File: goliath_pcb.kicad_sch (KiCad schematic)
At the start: 56 parts, among them IC1 MCT9001SD, IC2 MCT9001SD, IC3 MCT9001SD, IC4 MCT9001SD, IC5 MCT9001SD, IC6 MCT9001SD, IC7 MCT9001SD, J1 RJ45_LED, J2 RJ45_LED, J3 RJ45_LED, J4 RJ45_LED, U1 Pico, U2 LM7805_TO220, U3 74HCT244, U4 74HCT244, U5 LTC1298CS8-PBF

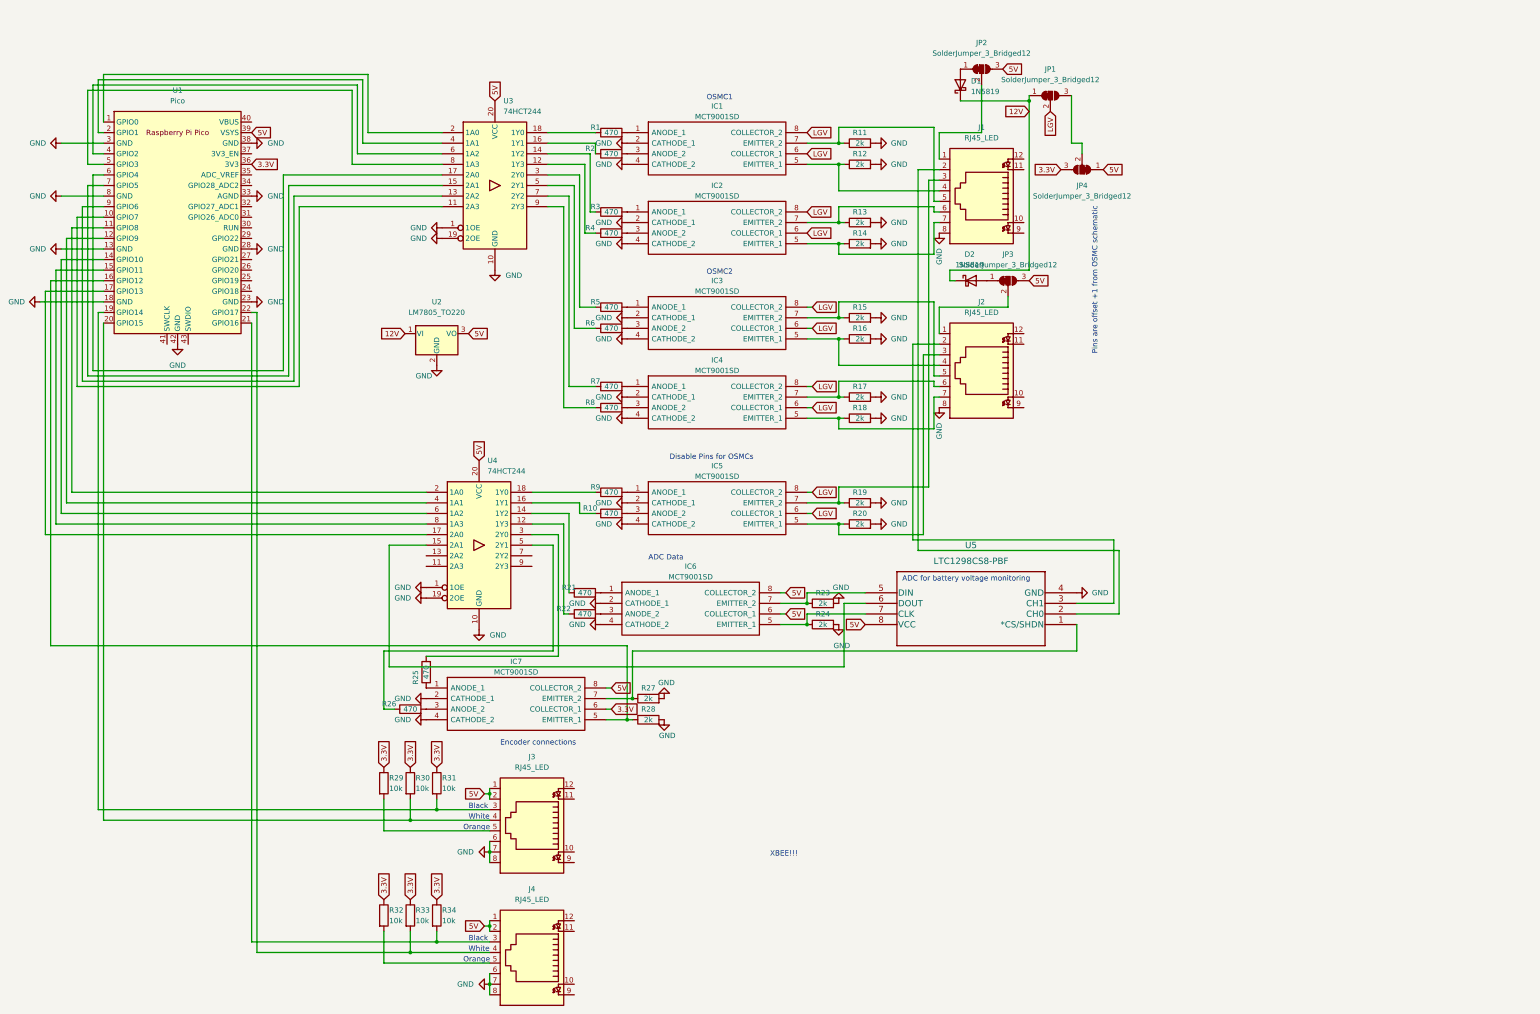
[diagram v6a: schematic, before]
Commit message: Add xBee initial plan
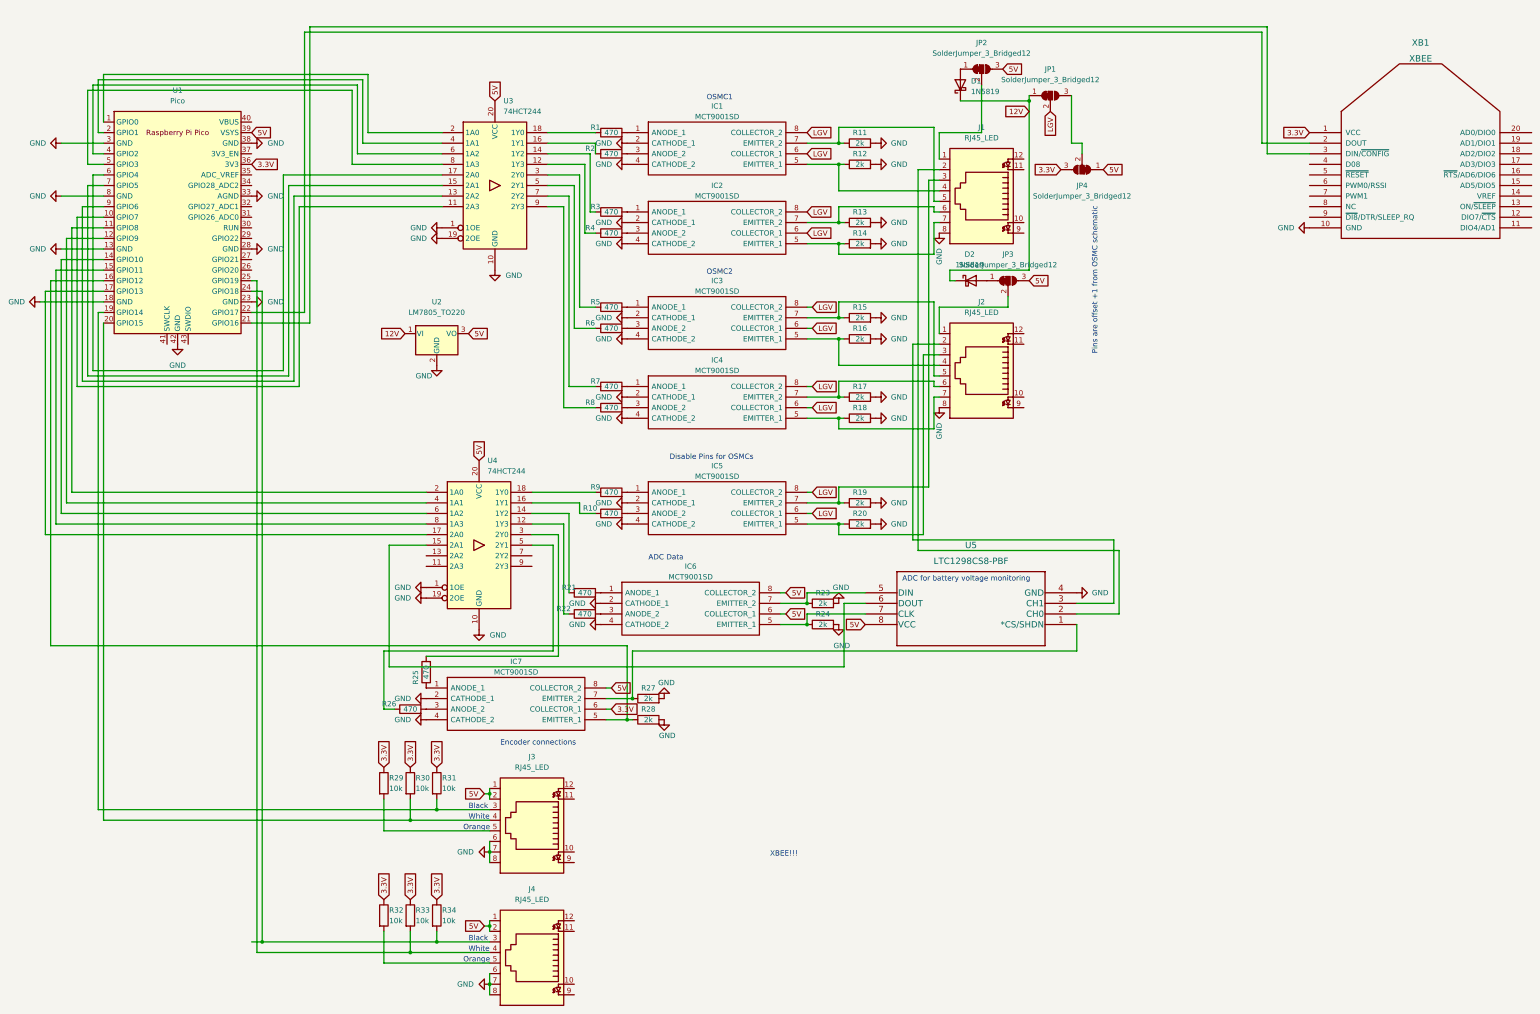
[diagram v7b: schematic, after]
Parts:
- added XB1: XBEE, RF_and_other_modules:XBEE_PRO_PTH, symbol RF_OEM_Parts:XBEE
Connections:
- net 3.3V: now also XB1.1 (VCC)
- net GND: now also XB1.10 (GND)
- net at J4.3, R34.2: now also U1.24 (GPIO18); no longer U1.21 (GPIO16)
- net at J4.4, R33.2: now also U1.25 (GPIO19); no longer U1.22 (GPIO17)
- new net: U1.22 (GPIO17), XB1.2 (DOUT)
- new net: U1.21 (GPIO16), XB1.3 (DIN/~{CONFIG})
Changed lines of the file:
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@@
   (junction (at 213.36 138.43) (diameter 0) (color 0 0 0 0)
   )
+  (junction (at 74.93 238.76) (diameter 0) (color 0 0 0 0)
+  )
   (junction (at 129.54 234.95) (diameter 0) (color 0 0 0 0)
   )
@@
     (stroke (width 0) (type default) (color 0 0 0 0))
   )
+  (wire (pts (xy 85.09 20.32) (xy 85.09 87.63))
+    (stroke (width 0) (type default) (color 0 0 0 0))
+  )
   (wire (pts (xy 144.78 168.91) (xy 104.14 168.91))
     (stroke (width 0) (type default) (color 0 0 0 0))
@@
     (stroke (width 0) (type default) (color 0 0 0 0))
   )
+  (wire (pts (xy 72.39 90.17) (xy 86.36 90.17))
+    (stroke (width 0) (type default) (color 0 0 0 0))
+  )
   (wire (pts (xy 24.13 80.01) (xy 24.13 167.64))
     (stroke (width 0) (type default) (color 0 0 0 0))
@@
     (stroke (width 0) (type default) (color 0 0 0 0))
   )
+  (wire (pts (xy 86.36 19.05) (xy 316.23 19.05))
+    (stroke (width 0) (type default) (color 0 0 0 0))
+  )
   (wire (pts (xy 219.71 157.48) (xy 214.63 157.48))
     (stroke (width 0) (type default) (color 0 0 0 0))
@@
     (stroke (width 0) (type default) (color 0 0 0 0))
   )
-  (wire (pts (xy 72.39 238.76) (xy 72.39 90.17))
-    (stroke (width 0) (type default) (color 0 0 0 0))
-  )
   (wire (pts (xy 36.83 41.91) (xy 36.83 30.48))
     (stroke (width 0) (type default) (color 0 0 0 0))
@@
     (stroke (width 0) (type default) (color 0 0 0 0))
   )
+  (wire (pts (xy 85.09 20.32) (xy 314.96 20.32))
+    (stroke (width 0) (type default) (color 0 0 0 0))
+  )
   (wire (pts (xy 104.14 212.09) (xy 104.14 204.47))
     (stroke (width 0) (type default) (color 0 0 0 0))
@@
     (stroke (width 0) (type default) (color 0 0 0 0))
   )
-  (wire (pts (xy 73.66 87.63) (xy 73.66 241.3))
-    (stroke (width 0) (type default) (color 0 0 0 0))
-  )
-  (wire (pts (xy 72.39 87.63) (xy 73.66 87.63))
-    (stroke (width 0) (type default) (color 0 0 0 0))
-  )
   (wire (pts (xy 25.4 138.43) (xy 114.3 138.43))
     (stroke (width 0) (type default) (color 0 0 0 0))
@@
     (stroke (width 0) (type default) (color 0 0 0 0))
   )
+  (wire (pts (xy 73.66 80.01) (xy 73.66 241.3))
+    (stroke (width 0) (type default) (color 0 0 0 0))
+  )
   (wire (pts (xy 214.63 157.48) (xy 214.63 172.72))
     (stroke (width 0) (type default) (color 0 0 0 0))
@@
     (stroke (width 0) (type default) (color 0 0 0 0))
   )
+  (wire (pts (xy 316.23 19.05) (xy 316.23 49.53))
+    (stroke (width 0) (type default) (color 0 0 0 0))
+  )
   (wire (pts (xy 104.14 168.91) (xy 104.14 182.88))
     (stroke (width 0) (type default) (color 0 0 0 0))
@@
     (stroke (width 0) (type default) (color 0 0 0 0))
   )
+  (wire (pts (xy 314.96 20.32) (xy 314.96 46.99))
+    (stroke (width 0) (type default) (color 0 0 0 0))
+  )
   (wire (pts (xy 143.51 44.45) (xy 154.94 44.45))
     (stroke (width 0) (type default) (color 0 0 0 0))
@@
     (stroke (width 0) (type default) (color 0 0 0 0))
   )
+  (wire (pts (xy 314.96 46.99) (xy 326.39 46.99))
+    (stroke (width 0) (type default) (color 0 0 0 0))
+  )
   (wire (pts (xy 116.84 207.01) (xy 35.56 207.01))
     (stroke (width 0) (type default) (color 0 0 0 0))
@@
     (stroke (width 0) (type default) (color 0 0 0 0))
   )
+  (wire (pts (xy 316.23 49.53) (xy 326.39 49.53))
+    (stroke (width 0) (type default) (color 0 0 0 0))
+  )
   (wire (pts (xy 205.74 160.02) (xy 205.74 162.56))
     (stroke (width 0) (type default) (color 0 0 0 0))
@@
     (stroke (width 0) (type default) (color 0 0 0 0))
   )
+  (wire (pts (xy 72.39 80.01) (xy 73.66 80.01))
+    (stroke (width 0) (type default) (color 0 0 0 0))
+  )
   (wire (pts (xy 241.3 80.01) (xy 240.03 80.01))
     (stroke (width 0) (type default) (color 0 0 0 0))
   )
+  (wire (pts (xy 74.93 238.76) (xy 74.93 82.55))
+    (stroke (width 0) (type default) (color 0 0 0 0))
+  )
   (wire (pts (xy 236.22 102.87) (xy 237.49 102.87))
     (stroke (width 0) (type default) (color 0 0 0 0))
@@
     (stroke (width 0) (type default) (color 0 0 0 0))
   )
+  (wire (pts (xy 72.39 87.63) (xy 85.09 87.63))
+    (stroke (width 0) (type default) (color 0 0 0 0))
+  )
   (wire (pts (xy 213.36 58.42) (xy 237.49 58.42))
     (stroke (width 0) (type default) (color 0 0 0 0))
@@
     (stroke (width 0) (type default) (color 0 0 0 0))
   )
+  (wire (pts (xy 74.93 238.76) (xy 72.39 238.76))
+    (stroke (width 0) (type default) (color 0 0 0 0))
+  )
   (wire (pts (xy 207.01 105.41) (xy 205.74 105.41))
     (stroke (width 0) (type default) (color 0 0 0 0))
@@
     (stroke (width 0) (type default) (color 0 0 0 0))
   )
-  (wire (pts (xy 116.84 238.76) (xy 72.39 238.76))
+  (wire (pts (xy 116.84 238.76) (xy 74.93 238.76))
     (stroke (width 0) (type default) (color 0 0 0 0))
   )
@@
     (stroke (width 0) (type default) (color 0 0 0 0))
   )
+  (wire (pts (xy 86.36 90.17) (xy 86.36 19.05))
+    (stroke (width 0) (type default) (color 0 0 0 0))
+  )
   (wire (pts (xy 162.56 185.42) (xy 162.56 167.64))
     (stroke (width 0) (type default) (color 0 0 0 0))
@@
     (stroke (width 0) (type default) (color 0 0 0 0))
   )
+  (wire (pts (xy 74.93 82.55) (xy 72.39 82.55))
+    (stroke (width 0) (type default) (color 0 0 0 0))
+  )
   (wire (pts (xy 213.36 71.12) (xy 213.36 73.66))
     (stroke (width 0) (type default) (color 0 0 0 0))
@@
     )
   )
+  (global_label "3.3V" (shape input) (at 326.39 44.45 180) (fields_autoplaced)
+    (effects (font (size 1.27 1.27)) (justify right))
+    (property "Intersheet References" "${INTERSHEET_REFS}" (id 0) (at 319.8645 44.3706 0)
+      (effects (font (size 1.27 1.27)) (justify right) hide)
+    )
+  )
   (symbol (lib_id "Device:R") (at 158.75 44.45 90) (unit 1)
     (in_bom yes) (on_board yes)
@@
     (pin "1")
   )
+  (symbol (lib_id "power:GND") (at 326.39 67.31 270) (unit 1)
+    (in_bom yes) (on_board yes)
+    (property "Reference" "#PWR0138" (id 0) (at 320.04 67.31 0)
+      (effects (font (size 1.27 1.27)) hide)
+    )
+    (property "Value" "GND" (id 1) (at 318.77 67.31 90)
+      (effects (font (size 1.27 1.27)) (justify left))
+    )
+    (property "Footprint" "" (id 2) (at 326.39 67.31 0)
+      (effects (font (size 1.27 1.27)) hide)
+    )
+    (property "Datasheet" "" (id 3) (at 326.39 67.31 0)
+      (effects (font (size 1.27 1.27)) hide)
+    )
+    (pin "1")
+  )
   (symbol (lib_id "power:GND") (at 237.49 110.49 0) (unit 1)
     (in_bom yes) (on_board yes)
@@
     (pin "8")
   )
+  (symbol (lib_id "RF_OEM_Parts:XBEE") (at 353.06 55.88 0) (unit 1)
+    (in_bom yes) (on_board yes) (fields_autoplaced)
+    (property "Reference" "XB1" (id 0) (at 353.06 22.86 0)
+      (effects (font (size 1.524 1.524)))
+    )
+    (property "Value" "XBEE" (id 1) (at 353.06 26.67 0)
+      (effects (font (size 1.524 1.524)))
+    )
+    (property "Footprint" "RF_and_other_modules:XBEE_PRO_PTH" (id 2) (at 353.06 55.88 0)
+      (effects (font (size 1.524 1.524)) hide)
+    )
+    (property "Datasheet" "" (id 3) (at 353.06 55.88 0)
+      (effects (font (size 1.524 1.524)))
+    )
+    (pin "1")
+    (pin "10")
+    (pin "11")
+    (pin "12")
+    (pin "13")
+    (pin "14")
+    (pin "15")
+    (pin "16")
+    (pin "17")
+    (pin "18")
+    (pin "19")
+    (pin "2")
+    (pin "20")
+    (pin "3")
+    (pin "4")
+    (pin "5")
+    (pin "6")
+    (pin "7")
+    (pin "8")
+    (pin "9")
+  )
   (symbol (lib_id "power:GND") (at 270.51 154.94 90) (unit 1)
     (in_bom yes) (on_board yes)
@@
       (reference "#PWR0137") (unit 1) (value "GND") (footprint "")
     )
+    (path "/241d0cce-0a89-4f69-9f2f-732e99ba3063"
+      (reference "#PWR0138") (unit 1) (value "GND") (footprint "")
+    )
     (path "/ceb69b8e-fe35-48d6-9c54-96ef6081dff2"
       (reference "D1") (unit 1) (value "1N5819") (footprint "Diode_THT:D_DO-41_SOD81_P10.16mm_Horizontal")
@@
       (reference "U5") (unit 1) (value "LTC1298CS8-PBF") (footprint "Package_DIP:DIP-8_W7.62mm_Socket")
     )
+    (path "/35241eab-8001-46c3-b2e4-04c58a50edd2"
+      (reference "XB1") (unit 1) (value "XBEE") (footprint "RF_and_other_modules:XBEE_PRO_PTH")
+    )
   )
